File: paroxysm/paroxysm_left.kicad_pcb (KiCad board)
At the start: 2 copper layers, 117.5 x 89.9 mm, 19 parts, among them SW10 SW_Push, SW11 SW_Push, SW12 SW_Push, SW14 SW_Push, SW15 SW_Push, SW16 SW_Push, SW17 SW_Push, SW18 SW_Push, SW20 SW_Push, SW21 SW_Push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

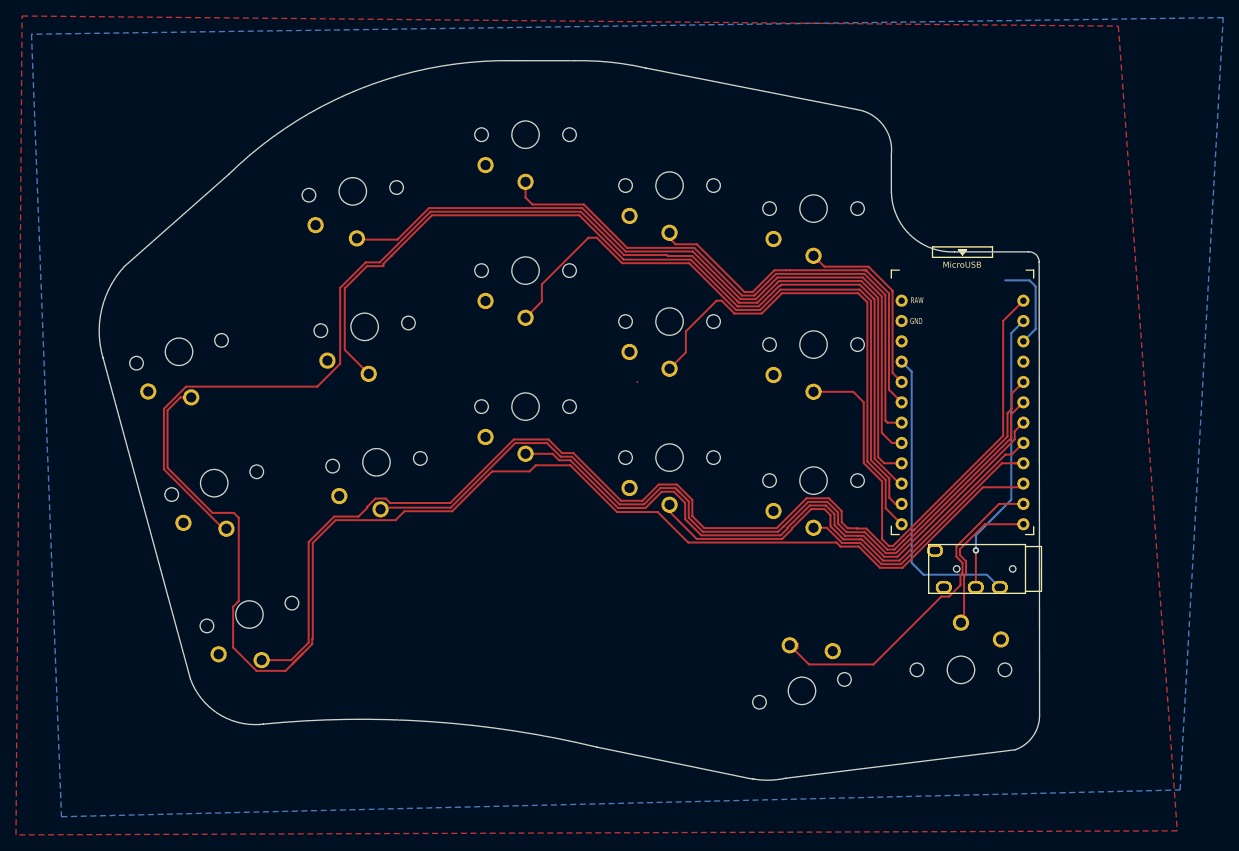
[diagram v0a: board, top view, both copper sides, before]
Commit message: Add original and one sided copies of paroxysm
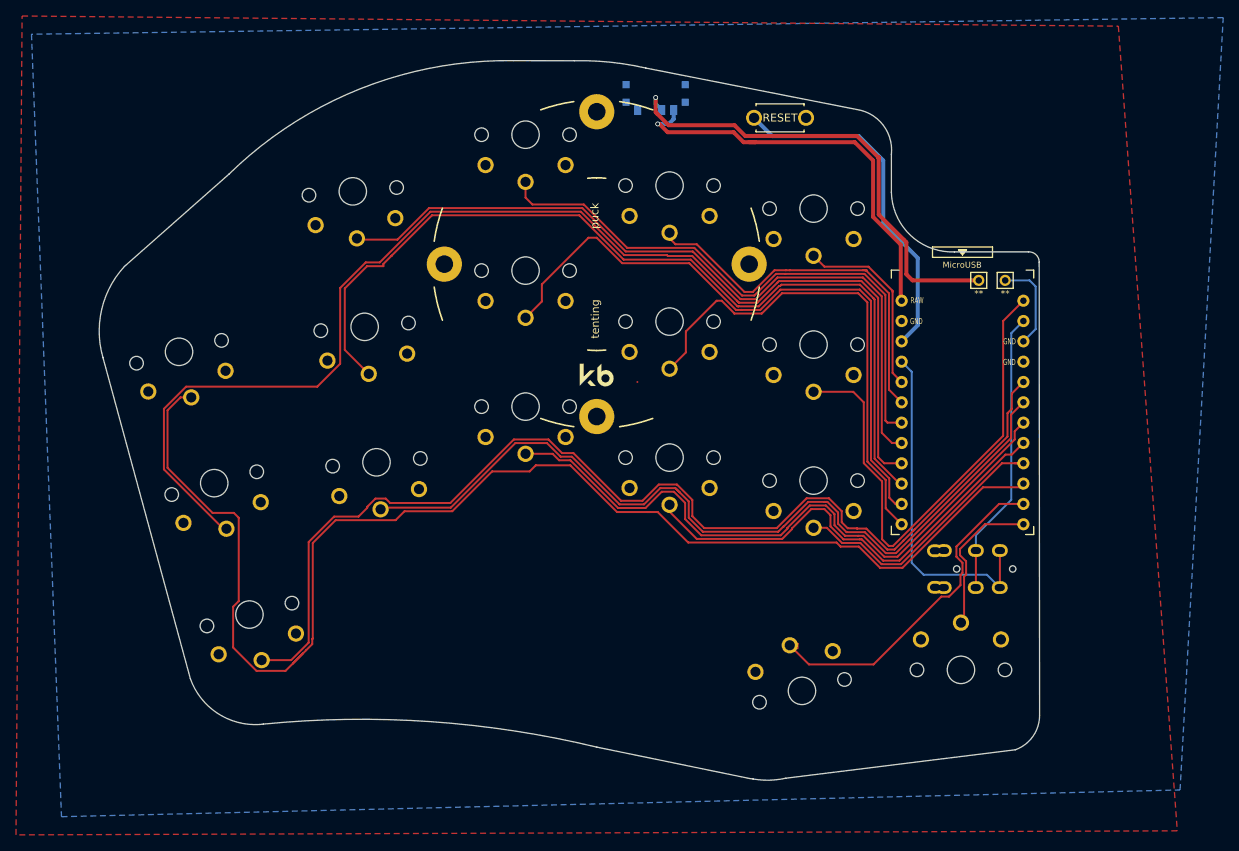
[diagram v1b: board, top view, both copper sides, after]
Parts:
- added **: Val**, kbd:1pin_conn, B.Cu at (207.8, 68.6)
- added BatGND1: MountingHole_Pad, kbd:1pin_conn, B.Cu at (204.5, 68.6)
- added REF**: Tenting Puck, kbd:Tenting_Puck2, F.Cu at (156.7, 66.5)
- added RSW1: SW_Push, kbd:ResetSW, F.Cu at (179.6, 48.3)
- added SW2: SW_SPDT, Kailh:SPDT_C128955r, B.Cu at (164.1, 45.2)
- Jack0: moved to B.Cu
- turned Jack0 to 90 degrees
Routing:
- net BT+: track 0.00 -> 59.5 mm, vias 0 -> 1
- net raw: track 0.15 -> 52.0 mm, vias 0 -> 1
- net reset: track 0.00 -> 44.1 mm
- net vcc: track 38.0 -> 42.6 mm
- net Switch18: track 35.8 -> 36.1 mm, vias 1 -> 0
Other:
- board text added: "15°"
- board text added: "5°"

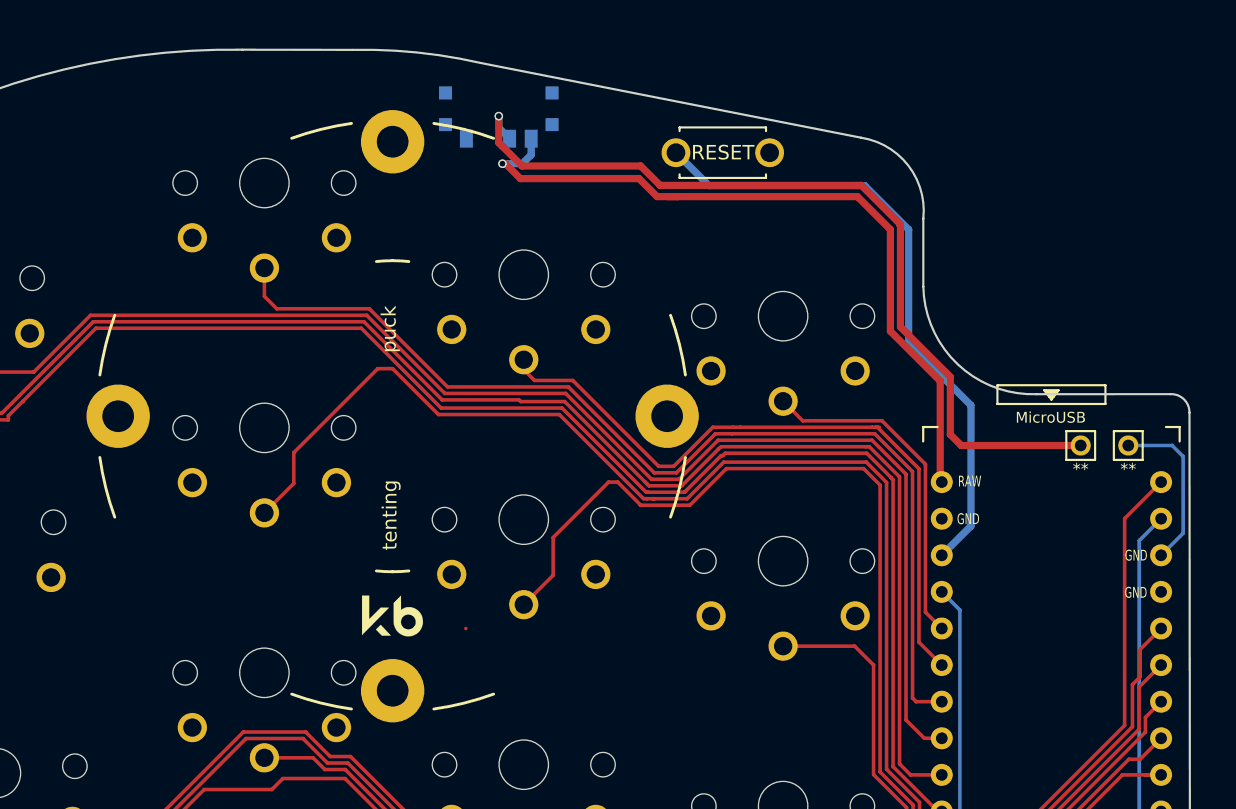
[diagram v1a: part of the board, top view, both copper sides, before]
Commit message: Remove paroxysm oneside, simplified paroxysm_left
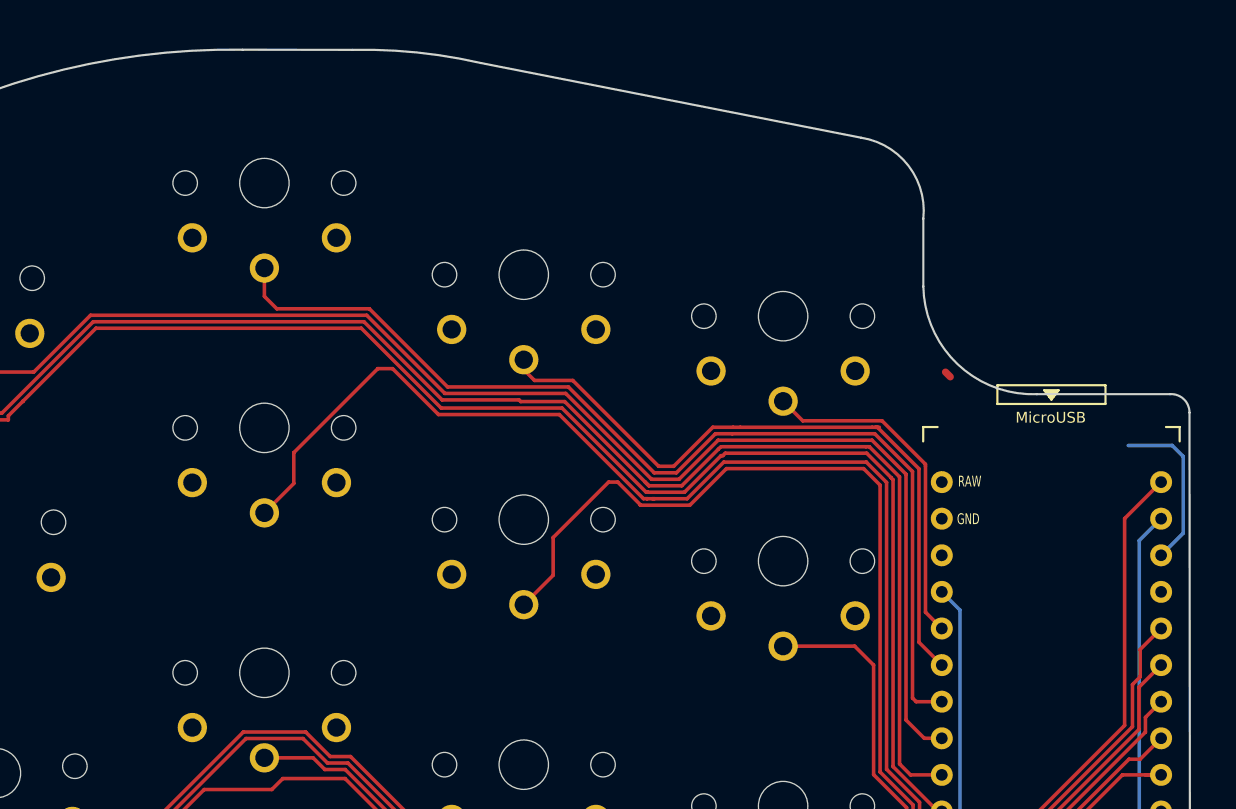
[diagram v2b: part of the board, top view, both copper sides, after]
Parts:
- removed **: Val**, kbd:1pin_conn
- removed BatGND1: MountingHole_Pad, kbd:1pin_conn
- removed REF**: Tenting Puck, kbd:Tenting_Puck2
- removed RSW1: SW_Push, kbd:ResetSW
- removed SW2: SW_SPDT, Kailh:SPDT_C128955r
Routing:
- net BT+: track 59.5 -> 0.47 mm, vias 1 -> 0
- net raw: track 52.0 -> 0.15 mm, vias 1 -> 0
- net reset: track 44.1 -> 0.00 mm
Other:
- board text removed: "15°"
- board text removed: "5°"
